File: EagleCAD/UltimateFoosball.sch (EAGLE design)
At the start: 28 parts

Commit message: Version 1 complete, sent to OSHPark
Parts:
- removed C7: (no value), adafruit:CPOL-USE5-13
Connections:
- net +5V: no longer C7.+
- net GND: no longer C7.-
- net RST_DISP: now also MS1.GPIO13
- net SCR_1_SIG: now also MS1.GPIOA1
- net SCR_2_SIG: now also MS1.GPIOA5
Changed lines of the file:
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@@
 <class number="0" name="default" width="0" drill="0">
+</class>
+<class number="1" name="H_PWR" width="0" drill="0">
+</class>
+<class number="2" name="3V_RAIL" width="0.4064" drill="0">
 </class>
 </classes>
@@
 <part name="C5" library="adafruit" library_urn="urn:adsk.eagle:library:420" deviceset="CPOL-US" device="E5-13" package3d_urn="urn:adsk.eagle:package:6240522/1"/>
 <part name="C6" library="adafruit" library_urn="urn:adsk.eagle:library:420" deviceset="CPOL-US" device="E5-13" package3d_urn="urn:adsk.eagle:package:6240522/1"/>
-<part name="C7" library="adafruit" library_urn="urn:adsk.eagle:library:420" deviceset="CPOL-US" device="E5-13" package3d_urn="urn:adsk.eagle:package:6240522/1"/>
 <part name="J2" library="SparkFun-Connectors" library_urn="urn:adsk.eagle:library:513" deviceset="CONN_02" device="PTH3" package3d_urn="urn:adsk.eagle:package:38048/1"/>
 <part name="J1" library="SparkFun-Connectors" library_urn="urn:adsk.eagle:library:513" deviceset="CONN_02" device="PTH3" package3d_urn="urn:adsk.eagle:package:38048/1"/>
@@
 <attribute name="VALUE" x="145.796" y="69.469" size="1.778" layer="96"/>
 </instance>
-<instance part="C7" gate="G$1" x="71.12" y="50.8" smashed="yes">
-<attribute name="NAME" x="72.136" y="51.435" size="1.778" layer="95"/>
-<attribute name="VALUE" x="72.136" y="46.609" size="1.778" layer="96"/>
-</instance>
 <instance part="J2" gate="G$1" x="185.42" y="147.32" smashed="yes">
 <attribute name="VALUE" x="182.88" y="142.494" size="1.778" layer="96" font="vector"/>
@@
 </segment>
 <segment>
-<wire x1="71.12" y1="45.72" x2="76.2" y2="45.72" width="0.1524" layer="91"/>
-<label x="76.2" y="45.72" size="1.27" layer="95" xref="yes"/>
-<pinref part="C7" gate="G$1" pin="-"/>
-</segment>
-<segment>
 <wire x1="215.9" y1="48.26" x2="213.36" y2="48.26" width="0.1524" layer="91"/>
 <label x="215.9" y="48.26" size="1.27" layer="95" xref="yes"/>
@@
 </segment>
 <segment>
-<label x="63.5" y="53.34" size="1.27" layer="95" rot="R180" xref="yes"/>
-<pinref part="C7" gate="G$1" pin="+"/>
-<wire x1="71.12" y1="53.34" x2="63.5" y2="53.34" width="0.1524" layer="91"/>
-</segment>
-<segment>
 <wire x1="215.9" y1="53.34" x2="213.36" y2="53.34" width="0.1524" layer="91"/>
 <label x="215.9" y="53.34" size="1.27" layer="95" xref="yes"/>
@@
 <wire x1="195.58" y1="165.1" x2="195.58" y2="162.56" width="0.1524" layer="91"/>
 <pinref part="J1" gate="G$1" pin="2"/>
+</segment>
+<segment>
+<pinref part="MS1" gate="G$1" pin="GPIO13"/>
+<wire x1="96.52" y1="142.24" x2="91.44" y2="142.24" width="0.1524" layer="91"/>
+<label x="96.52" y="142.24" size="1.27" layer="95" xref="yes"/>
 </segment>
 </net>
@@
 <junction x="144.78" y="142.24"/>
 </segment>
+<segment>
+<pinref part="MS1" gate="G$1" pin="GPIOA5"/>
+<wire x1="40.64" y1="137.16" x2="48.26" y2="137.16" width="0.1524" layer="91"/>
+<label x="40.64" y="137.16" size="1.27" layer="95" rot="R180" xref="yes"/>
+</segment>
 </net>
 <net name="SCR_1_SIG" class="0">
@@
 <junction x="116.84" y="157.48"/>
 </segment>
+<segment>
+<pinref part="MS1" gate="G$1" pin="GPIOA1"/>
+<wire x1="40.64" y1="147.32" x2="48.26" y2="147.32" width="0.1524" layer="91"/>
+<label x="40.64" y="147.32" size="1.27" layer="95" rot="R180" xref="yes"/>
+</segment>
 </net>
 <net name="N$2" class="0">
@@
 </segment>
 </net>
-<net name="+3V" class="0">
+<net name="+3V" class="2">
 <segment>
 <pinref part="MUSIC_WING" gate="G$1" pin="3V"/>

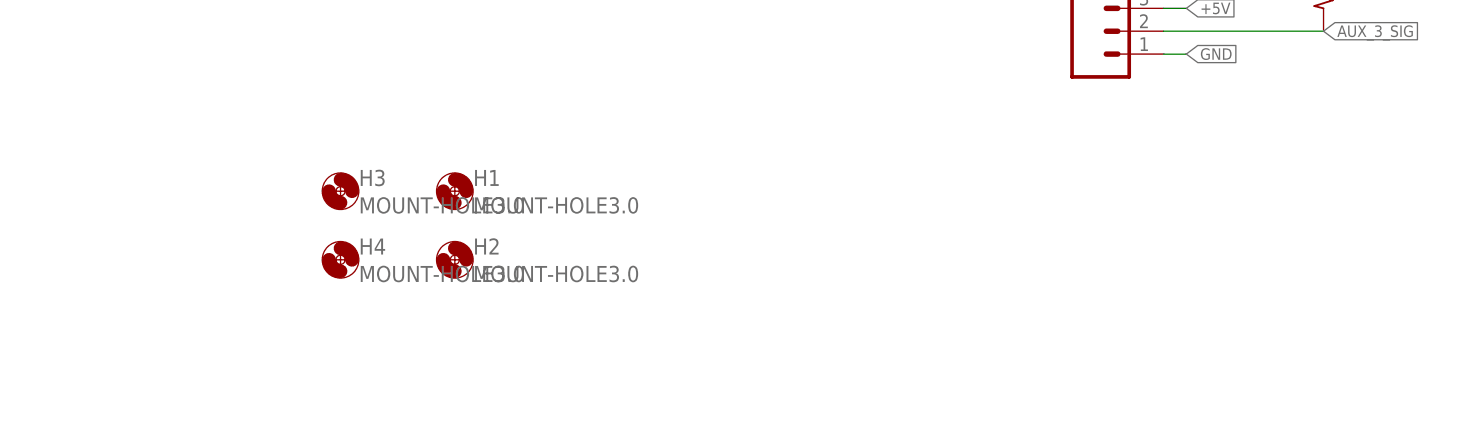
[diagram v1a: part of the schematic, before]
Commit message: added game over sounds/logic and update order of scoreboard updating
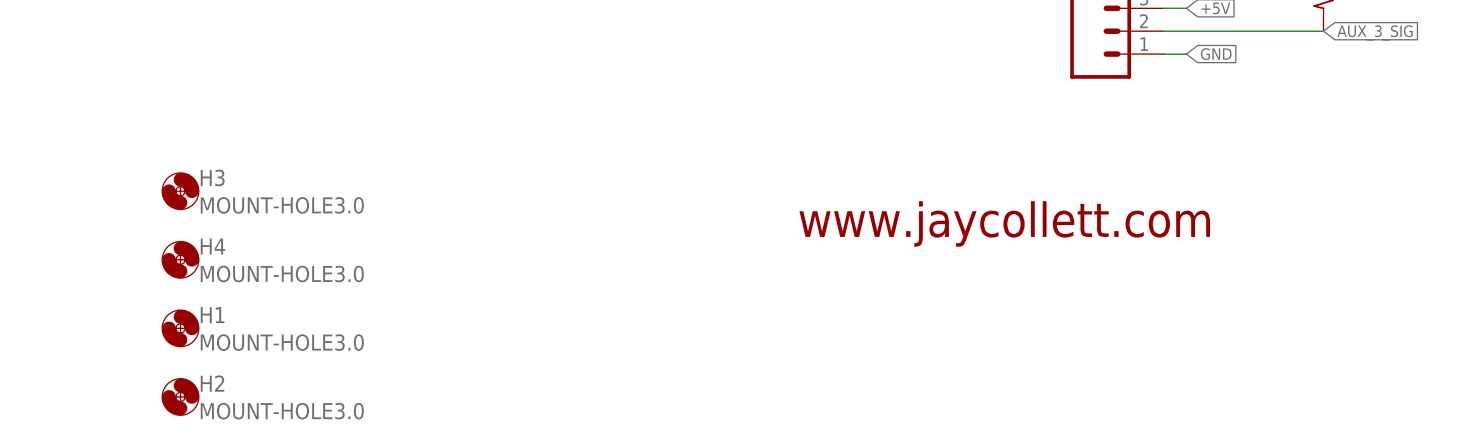
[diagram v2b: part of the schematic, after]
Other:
- note added: "www.jaycollett.com"
- moved on the sheet: H1, H2, H3, H4
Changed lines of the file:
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@@
 <sheet>
 <plain>
+<text x="172.72" y="27.94" size="3.81" layer="94">www.jaycollett.com</text>
 </plain>
 <instances>
@@
 <attribute name="NAME" x="203.2" y="56.388" size="1.778" layer="95" font="vector"/>
 </instance>
-<instance part="H1" gate="G$1" x="134.62" y="33.02" smashed="yes">
-<attribute name="NAME" x="136.652" y="33.6042" size="1.778" layer="95"/>
-<attribute name="VALUE" x="136.652" y="30.5562" size="1.778" layer="96"/>
+<instance part="H1" gate="G$1" x="104.14" y="17.78" smashed="yes">
+<attribute name="NAME" x="106.172" y="18.3642" size="1.778" layer="95"/>
+<attribute name="VALUE" x="106.172" y="15.3162" size="1.778" layer="96"/>
 </instance>
-<instance part="H2" gate="G$1" x="134.62" y="25.4" smashed="yes">
-<attribute name="NAME" x="136.652" y="25.9842" size="1.778" layer="95"/>
-<attribute name="VALUE" x="136.652" y="22.9362" size="1.778" layer="96"/>
+<instance part="H2" gate="G$1" x="104.14" y="10.16" smashed="yes">
+<attribute name="NAME" x="106.172" y="10.7442" size="1.778" layer="95"/>
+<attribute name="VALUE" x="106.172" y="7.6962" size="1.778" layer="96"/>
 </instance>
-<instance part="H3" gate="G$1" x="121.92" y="33.02" smashed="yes">
-<attribute name="NAME" x="123.952" y="33.6042" size="1.778" layer="95"/>
-<attribute name="VALUE" x="123.952" y="30.5562" size="1.778" layer="96"/>
+<instance part="H3" gate="G$1" x="104.14" y="33.02" smashed="yes">
+<attribute name="NAME" x="106.172" y="33.6042" size="1.778" layer="95"/>
+<attribute name="VALUE" x="106.172" y="30.5562" size="1.778" layer="96"/>
 </instance>
-<instance part="H4" gate="G$1" x="121.92" y="25.4" smashed="yes">
-<attribute name="NAME" x="123.952" y="25.9842" size="1.778" layer="95"/>
-<attribute name="VALUE" x="123.952" y="22.9362" size="1.778" layer="96"/>
+<instance part="H4" gate="G$1" x="104.14" y="25.4" smashed="yes">
+<attribute name="NAME" x="106.172" y="25.9842" size="1.778" layer="95"/>
+<attribute name="VALUE" x="106.172" y="22.9362" size="1.778" layer="96"/>
 </instance>
 </instances>
